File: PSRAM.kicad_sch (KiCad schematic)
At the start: 0 parts

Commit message: OCTOSPI Pinout
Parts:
- added U2: W958D8NBYA5I, BR_IC:BGA-24_6x8mm_Layout5x5_P1.0mm, symbol BR_IC:W958D8NBYA5I

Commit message: updates
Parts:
- added R1, R10, R11, R12, R13, R14, R16, R17, R19, R2, R3, R7, R9: 100R, BR_Passives:C_0402_1005Metric-minimized, symbol BR_Resistors_0402:R_0402_100R
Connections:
- net at U2.A3 (~{CS}): now also R1.2
- net at U2.A4 (~{RESET}): now also R2.2
- net at U2.B1 (~{CK}): now also R3.1
- net at U2.B2 (CK): now also R7.2
- net GND: now reaches U2.B3 (VSS)
- net GND: now also U2.C1 (VSSQ), U2.E5 (VSSQ)
- net at U2.C3 (RWDS): now also R9.2
- net at U2.C4 (DQ2): now also R12.1
- net at U2.D2 (DQ1): now also R11.1
- net at U2.D3 (DQ0): now also R10.1
- net at U2.D4 (DQ3): now also R13.1
- net at U2.D5 (DQ4): now also R14.1
- net at U2.E1 (DQ7): now also R19.1
- net at U2.E2 (DQ6): now also R17.2
- net at U2.E3 (DQ5): now also R16.1
- new net OCTOSPI1.CLK: R7.1
- new net OCTOSPI1.DQS: R9.1
- new net OCTOSPI1.IO0: R10.2
- new net OCTOSPI1.IO1: R11.2
- new net OCTOSPI1.IO2: R12.2
- new net OCTOSPI1.IO3: R13.2
- new net OCTOSPI1.IO4: R14.2
- new net OCTOSPI1.IO5: R16.2
- new net OCTOSPI1.IO6: R17.1
- new net OCTOSPI1.IO7: R19.2
- new net OCTOSPI1.NCLK: R3.2
- new net OCTOSPI1.NCS: R1.1
- new net PSRAM_nRST: R2.1
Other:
- moved on the sheet: U2

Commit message: various updates + digital drive sheet
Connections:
- net 1V8: now reaches U2.B4 (VCC)
- net 1V8: now also U2.D1 (VCCQ), U2.E4 (VCCQ)
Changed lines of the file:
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@@
+	)
+	(junction
+		(at 148.59 59.69)
+		(diameter 0)
+		(color 0 0 0 0)
+	)
+	(junction
+		(at 151.13 59.69)
+		(diameter 0)
+		(color 0 0 0 0)
 	)
 	(junction
@@
 	(wire
 		(pts
+			(xy 148.59 59.69) (xy 151.13 59.69)
+		)
+		(stroke
+			(width 0)
+			(type default)
+		)
+	)
+	(wire
+		(pts
 			(xy 148.59 106.68) (xy 148.59 104.14)
 		)
@@
 	(wire
 		(pts
+			(xy 151.13 59.69) (xy 151.13 63.5)
+		)
+		(stroke
+			(width 0)
+			(type default)
+		)
+	)
+	(wire
+		(pts
 			(xy 165.1 86.36) (xy 190.5 86.36)
 		)
@@
 	(wire
 		(pts
+			(xy 148.59 59.69) (xy 148.59 63.5)
+		)
+		(stroke
+			(width 0)
+			(type default)
+		)
+	)
+	(wire
+		(pts
 			(xy 67.31 35.56) (xy 92.71 35.56)
 		)
@@
 	(wire
 		(pts
+			(xy 154.94 63.5) (xy 154.94 59.69)
+		)
+		(stroke
+			(width 0)
+			(type default)
+		)
+	)
+	(wire
+		(pts
 			(xy 67.31 55.88) (xy 92.71 55.88)
 		)
@@
 	(wire
 		(pts
+			(xy 137.16 59.69) (xy 148.59 59.69)
+		)
+		(stroke
+			(width 0)
+			(type default)
+		)
+	)
+	(wire
+		(pts
 			(xy 165.1 91.44) (xy 190.5 91.44)
+		)
+		(stroke
+			(width 0)
+			(type default)
+		)
+	)
+	(wire
+		(pts
+			(xy 151.13 59.69) (xy 154.94 59.69)
 		)
 		(stroke
@@
 			)
 			(justify right bottom)
+		)
+	)
+	(label "1V8"
+		(at 139.7 59.69 0)
+		(effects
+			(font
+				(size 1.27 1.27)
+			)
+			(justify left bottom)
 		)
 	)
@@
 		(effects
 			(font
+				(size 1.27 1.27)
+			)
+			(justify right)
+		)
+	)
+	(hierarchical_label "1V8"
+		(shape input)
+		(at 137.16 59.69 180)
+		(effects
+			(font

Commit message: a bunch of updates
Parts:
- U2: value W958D8NBYA5I -> S27KL0642DPBHB023; symbol BR_IC:W958D8NBYA5I -> BR_IC:S27KL0642DPBHB023; BRE Number BRE-001208 -> BRE-001273; JLCPCB Part Num C7420405 -> C5157921; LCSC Part C7420405 -> C5157921; Manufacturer Winbond Electronics -> Infineon Technologies; Manufacturer Part Num W958D8NBYA5I -> S27KL0642DPBHB023
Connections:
- net 1V8 renamed 3V3
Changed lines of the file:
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@@
 		)
 	)
-	(label "1V8"
+	(label "3V3"
 		(at 139.7 59.69 0)
 		(effects
@@
 		)
 	)
-	(hierarchical_label "1V8"
+	(hierarchical_label "3V3"
 		(shape input)
 		(at 137.16 59.69 180)
@@
 	)
 	(symbol
-		(lib_id "BR_IC:W958D8NBYA5I")
+		(lib_id "BR_IC:S27KL0642DPBHB023")
 		(at 151.13 83.82 0)
 		(unit 1)
@@
 			)
 		)
-		(property "Value" "W958D8NBYA5I"
+		(property "Value" "S27KL0642DPBHB023"
 			(at 157.0833 63.5 0)
 			(effects
@@
 			)
 		)
-		(property "Datasheet" "https://www.winbond.com/resource-files/W958D8NBYA%20256Mb%20HyperRAM%20TFBGA24%20SDP%2085C%20datasheet_A01-003_20220630.pdf"
+		(property "Datasheet" "https://www.infineon.com/assets/row/public/documents/10/49/infineon-s27kl0642-s27ks0642-3.0-v-1.8-v-64-mb-8-mb-hyperram-self-refresh-dram-datasheet-en.pdf?fileId=8ac78c8c7d0d8da4017d0ee8a1c47164"
 			(at 151.13 10.16 0)
 			(effects
@@
 			)
 		)
-		(property "Description" "PSRAM (Pseudo SRAM) Memory IC 256Mbit HyperBus 200MHz 35ns 24-TFBGA (6x8)"
+		(property "Description" "PSRAM (Pseudo SRAM) Memory IC 64Mbit HyperBus 166 MHz 36 ns 24-FBGA (6x8)"
 			(at 151.13 12.7 0)
 			(effects
@@
 			)
 		)
-		(property "Manufacturer" "Winbond Electronics"
+		(property "Manufacturer" "Infineon Technologies"
 			(at 151.13 15.24 0)
 			(effects
@@
 			)
 		)
-		(property "Manufacturer Part Num" "W958D8NBYA5I"
+		(property "Manufacturer Part Num" "S27KL0642DPBHB023"
 			(at 151.13 17.78 0)
 			(effects
@@
 			)
 		)
-		(property "BRE Number" "BRE-001208"
+		(property "BRE Number" " BRE-001273"
 			(at 151.13 20.32 0)
 			(effects
@@
 			)
 		)
-		(property "LCSC Part" " C7420405"
+		(property "LCSC Part" "C5157921"
 			(at 151.13 22.86 0)
 			(effects
@@
 			)
 		)
-		(property "JLCPCB Part Num" " C7420405"
+		(property "JLCPCB Part Num" "C5157921"
 			(at 151.13 25.4 0)
 			(effects

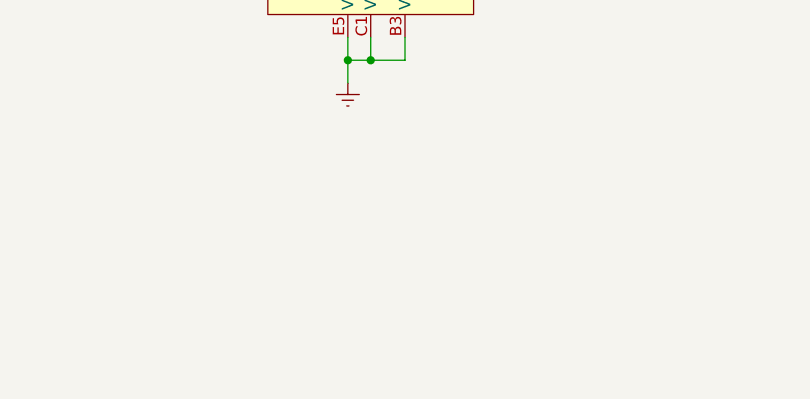
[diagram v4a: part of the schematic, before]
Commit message: added rj45 and h-bridge + stm pinout spreadsheet
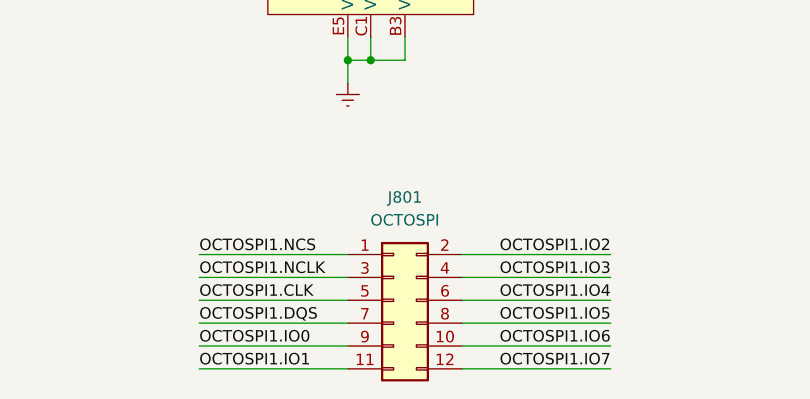
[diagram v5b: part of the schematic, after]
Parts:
- added J801: OCTOSPI, BR_Connectors:PinHeader_2x06_P2.54mm_Vertical_SMD, symbol BR_Connectors_Header:Header_Pin_02x06_2.54mm_Vert_SMD
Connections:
- net OCTOSPI1.CLK: now also J801.5 (Pin_5)
- net OCTOSPI1.DQS: now also J801.7 (Pin_7)
- net OCTOSPI1.IO0: now also J801.9 (Pin_9)
- net OCTOSPI1.IO1: now also J801.11 (Pin_9)
- net OCTOSPI1.IO2: now also J801.2 (Pin_2)
- net OCTOSPI1.IO3: now also J801.4 (Pin_4)
- net OCTOSPI1.IO4: now also J801.6 (Pin_6)
- net OCTOSPI1.IO5: now also J801.8 (Pin_8)
- net OCTOSPI1.IO6: now also J801.10 (Pin_10)
- net OCTOSPI1.IO7: now also J801.12 (Pin_9)
- net OCTOSPI1.NCLK: now also J801.3 (Pin_3)
- net OCTOSPI1.NCS: now also J801.1 (Pin_1)

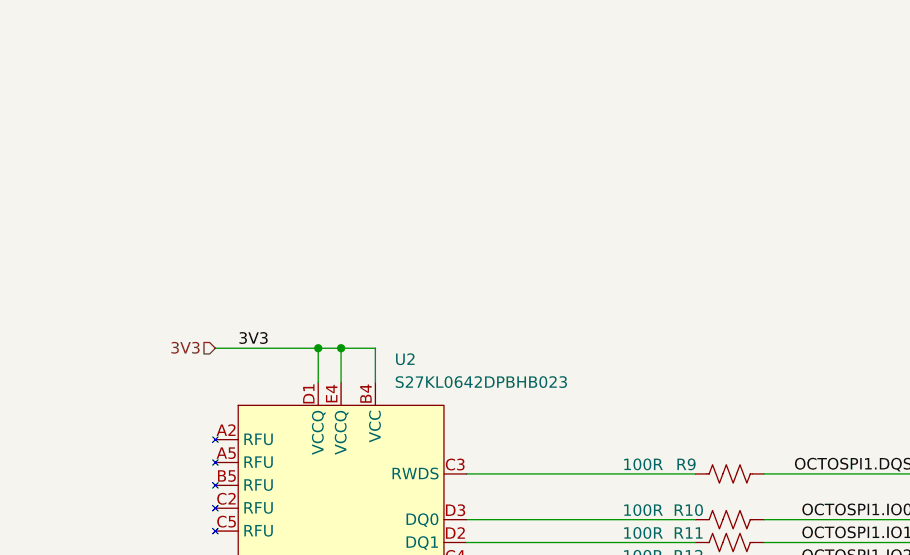
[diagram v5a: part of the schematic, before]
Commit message: implementing feedback + added stepper driver
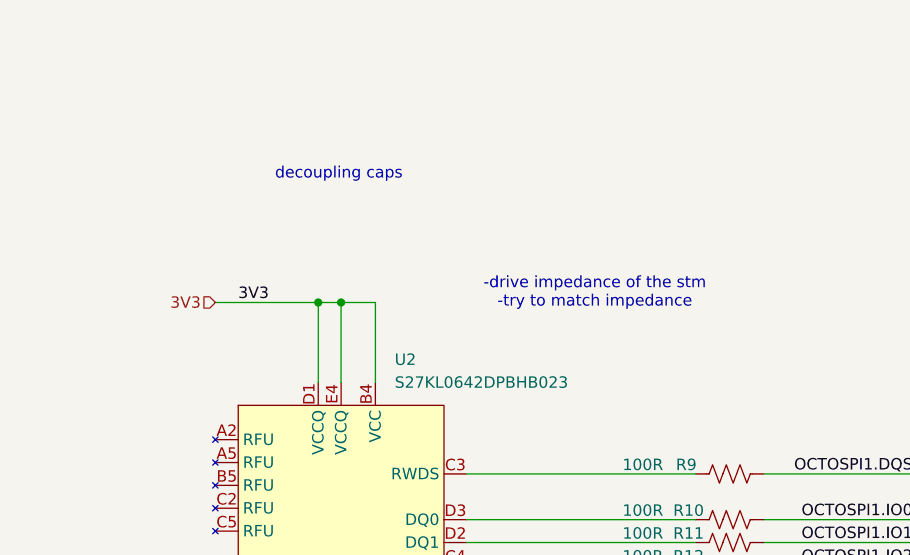
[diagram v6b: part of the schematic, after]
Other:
- note added: "-drive impedance of the stm -try to match impedance"
- note added: "decoupling caps"
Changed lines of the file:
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@@
 	(generator_version "9.0")
 	(paper "A4")
+	(text "decoupling caps"
+		(exclude_from_sim no)
+		(at 150.876 40.386 0)
+		(effects
+			(font
+				(size 1.27 1.27)
+				(color 170 109 255 1)
+			)
+		)
+	)
+	(text "-drive impedance of the stm\n-try to match impedance"
+		(exclude_from_sim no)
+		(at 179.324 53.594 0)
+		(effects
+			(font
+				(size 1.27 1.27)
+			)
+		)
+	)
+	(junction
+		(at 148.59 54.61)
+		(diameter 0)
+		(color 0 0 0 0)
+	)
 	(junction
 		(at 148.59 106.68)
@@
 	)
 	(junction
-		(at 148.59 59.69)
-		(diameter 0)
-		(color 0 0 0 0)
-	)
-	(junction
-		(at 151.13 59.69)
+		(at 151.13 54.61)
 		(diameter 0)
 		(color 0 0 0 0)
@@
 	(wire
 		(pts
-			(xy 148.59 59.69) (xy 151.13 59.69)
+			(xy 151.13 54.61) (xy 151.13 63.5)
 		)
 		(stroke
@@
 	(wire
 		(pts
-			(xy 151.13 59.69) (xy 151.13 63.5)
-		)
-		(stroke
-			(width 0)
-			(type default)
-		)
-	)
-	(wire
-		(pts
 			(xy 132.08 133.35) (xy 148.59 133.35)
 		)
@@
 	(wire
 		(pts
-			(xy 148.59 59.69) (xy 148.59 63.5)
-		)
-		(stroke
-			(width 0)
-			(type default)
-		)
-	)
-	(wire
-		(pts
 			(xy 67.31 35.56) (xy 92.71 35.56)
 		)
@@
 	(wire
 		(pts
-			(xy 154.94 63.5) (xy 154.94 59.69)
+			(xy 154.94 63.5) (xy 154.94 54.61)
 		)
 		(stroke
@@
 	(wire
 		(pts
-			(xy 137.16 59.69) (xy 148.59 59.69)
+			(xy 137.16 54.61) (xy 148.59 54.61)
 		)
 		(stroke
@@
 	(wire
 		(pts
-			(xy 151.13 59.69) (xy 154.94 59.69)
+			(xy 151.13 54.61) (xy 154.94 54.61)
 		)
 		(stroke
@@
 	(wire
 		(pts
+			(xy 148.59 54.61) (xy 148.59 63.5)
+		)
+		(stroke
+			(width 0)
+			(type default)
+		)
+	)
+	(wire
+		(pts
 			(xy 198.12 93.98) (xy 214.63 93.98)
 		)
@@
 		(pts
 			(xy 198.12 81.28) (xy 214.63 81.28)
+		)
+		(stroke
+			(width 0)
+			(type default)
+		)
+	)
+	(wire
+		(pts
+			(xy 148.59 54.61) (xy 151.13 54.61)
 		)
 		(stroke
@@
 	)
 	(label "3V3"
-		(at 139.7 59.69 0)
+		(at 139.7 54.61 0)
 		(effects
 			(font
@@
 	(hierarchical_label "3V3"
 		(shape input)
-		(at 137.16 59.69 180)
-		(effects
-			(font
+		(at 137.16 54.61 180)
+		(effects
+			(font

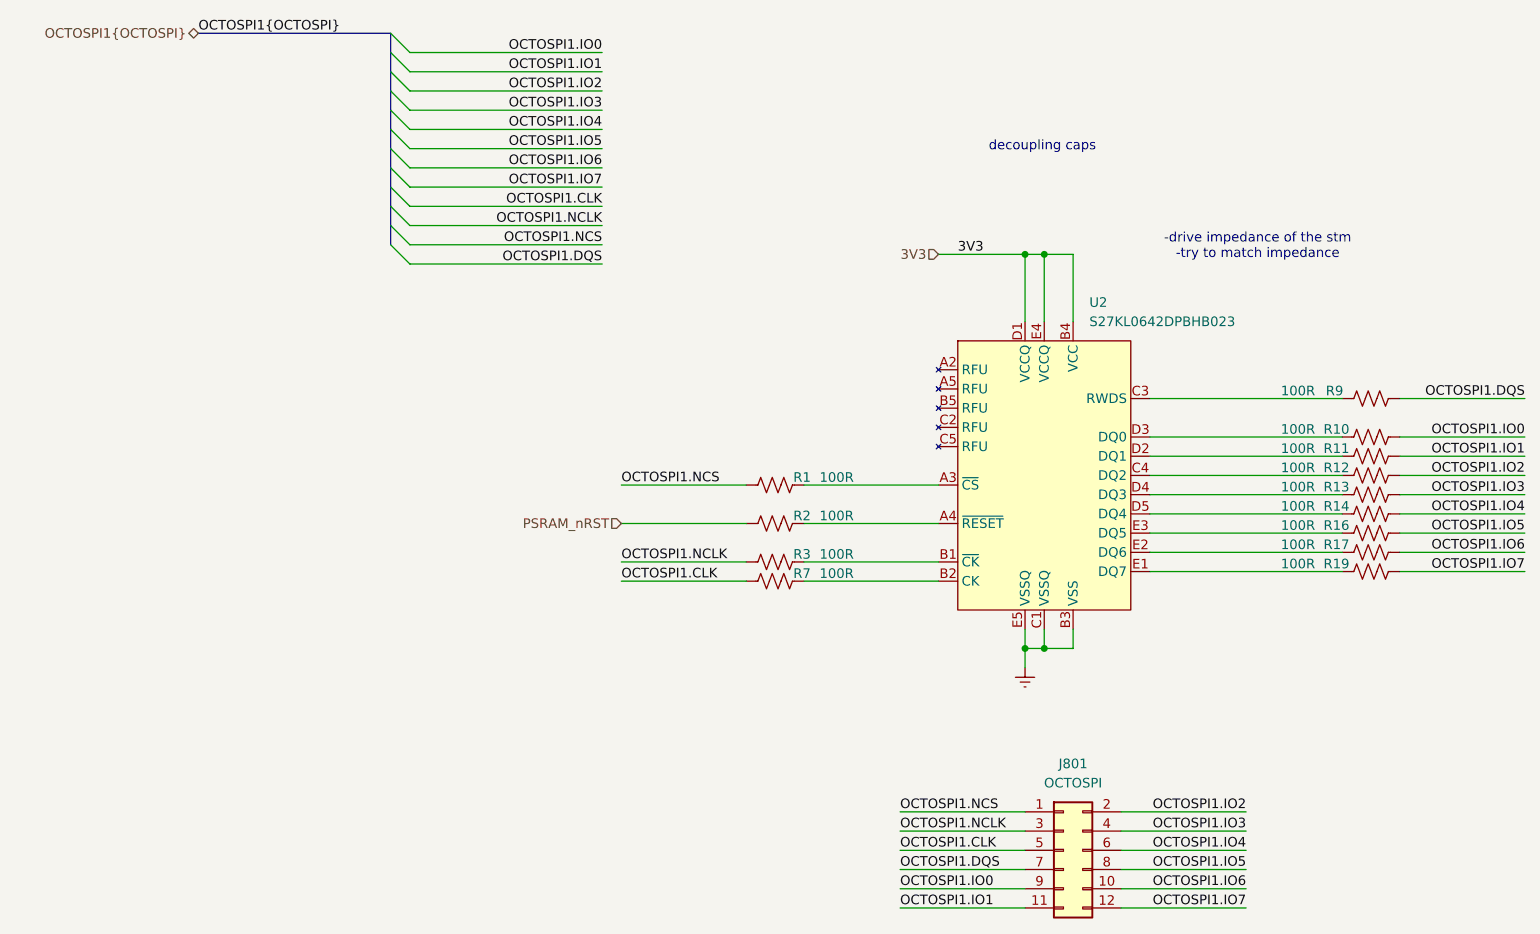
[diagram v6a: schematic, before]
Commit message: completed feedback from review + reannotated sheets
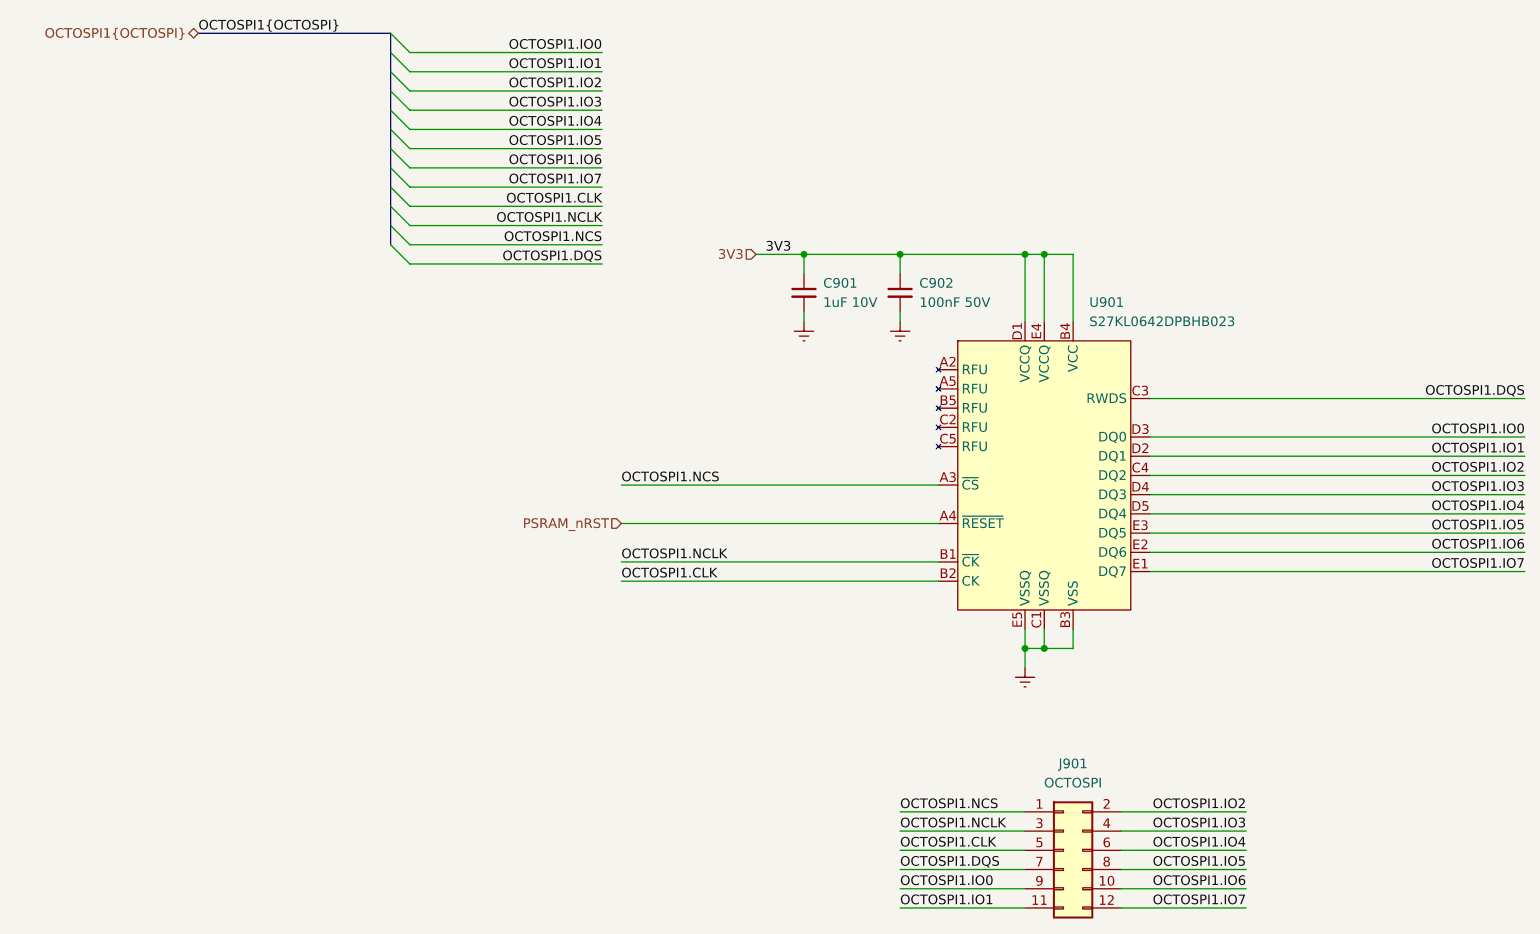
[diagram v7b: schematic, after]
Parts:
- removed R1, R10, R11, R12, R13, R14, R16, R17, R19, R2, R3, R7, R9: 100R, BR_Passives:C_0402_1005Metric-minimized, symbol BR_Resistors_0402:R_0402_100R
- added C901: 1uF 10V, BR_Passives:C_0402_1005Metric-minimized, symbol BR_Capacitors_0402:C_0402_1uF_10V_X7R_10%
- added C902: 100nF 50V, BR_Passives:C_0402_1005Metric-minimized, symbol BR_Capacitors_0402:C_0402_100nF_50V_X7R_10%_AEC-Q200
- renumbered J801 to J901, U2 to U901
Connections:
- net 3V3: now also C901.1, C902.1
- net GND: now also C901.2, C902.2
- net OCTOSPI1.CLK: now also U901.B2 (CK)
- net OCTOSPI1.DQS: now also U901.C3 (RWDS)
- net OCTOSPI1.IO0: now also U901.D3 (DQ0)
- net OCTOSPI1.IO1: now also U901.D2 (DQ1)
- net OCTOSPI1.IO2: now also U901.C4 (DQ2)
- net OCTOSPI1.IO3: now also U901.D4 (DQ3)
- net OCTOSPI1.IO4: now also U901.D5 (DQ4)
- net OCTOSPI1.IO5: now also U901.E3 (DQ5)
- net OCTOSPI1.IO6: now also U901.E2 (DQ6)
- net OCTOSPI1.IO7: now also U901.E1 (DQ7)
- net OCTOSPI1.NCLK: now also U901.B1 (~{CK})
- net OCTOSPI1.NCS: now also U901.A3 (~{CS})
- net PSRAM_nRST: now also U901.A4 (~{RESET})
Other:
- note removed: "-drive impedance of the stm -try to match impedance"
- note removed: "decoupling caps"
